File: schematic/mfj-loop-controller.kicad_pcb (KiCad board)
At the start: 4 copper layers, 120.6 x 91.4 mm, 34 parts, among them J1 Adafruit ADS1115, J2 Bias Tee, J3 SWR Bridge, J4 DC+12V, U1 AD8032, U2 R-785.0-1.0, U3 TMR3-1212, U4 WeMos_D1_mini, U5 LCC120, U6 LCC120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

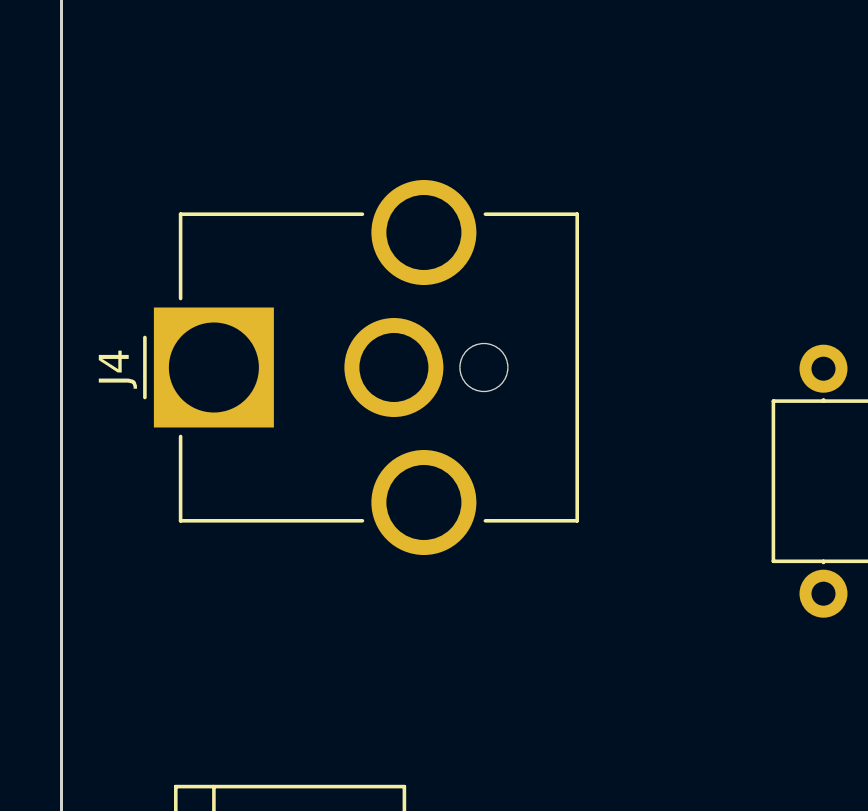
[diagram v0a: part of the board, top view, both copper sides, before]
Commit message: Rotate power jack 180 degrees on PCB.
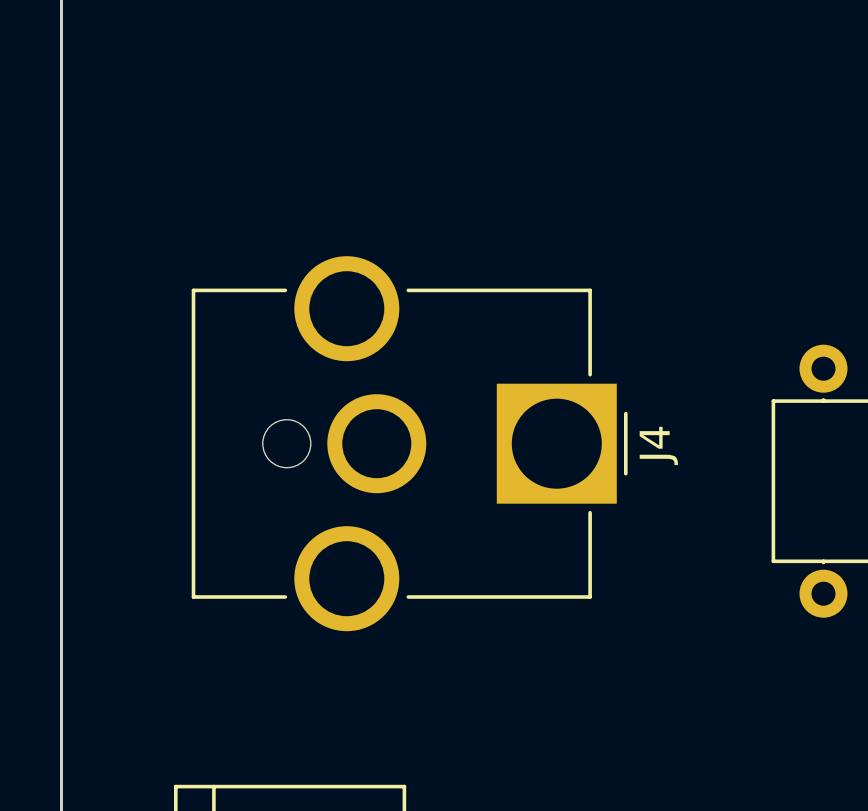
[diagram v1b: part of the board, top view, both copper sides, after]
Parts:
- moved J4 11.7 mm to (74.9, 53.3), turned to 270 degrees

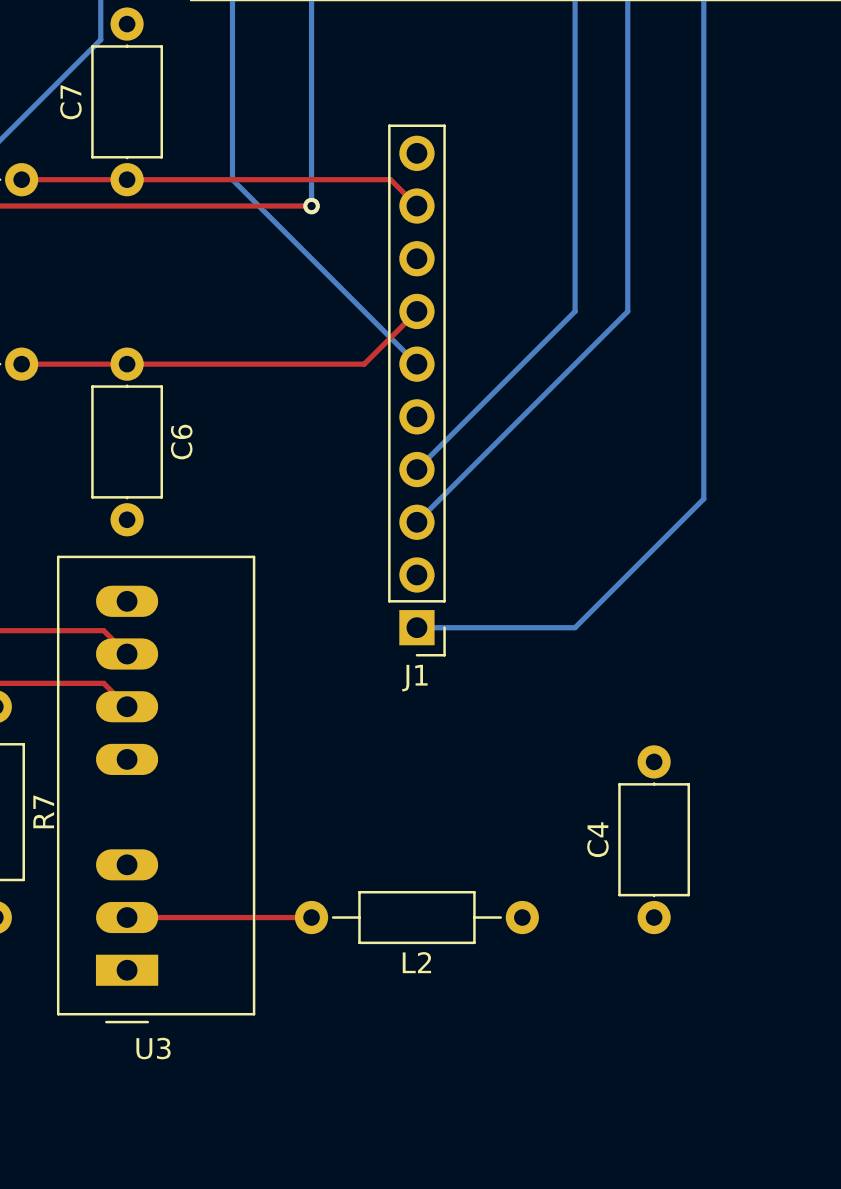
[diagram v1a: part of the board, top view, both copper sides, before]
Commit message: Add minimum load to 12V isolated supply to reduce tuning noise.
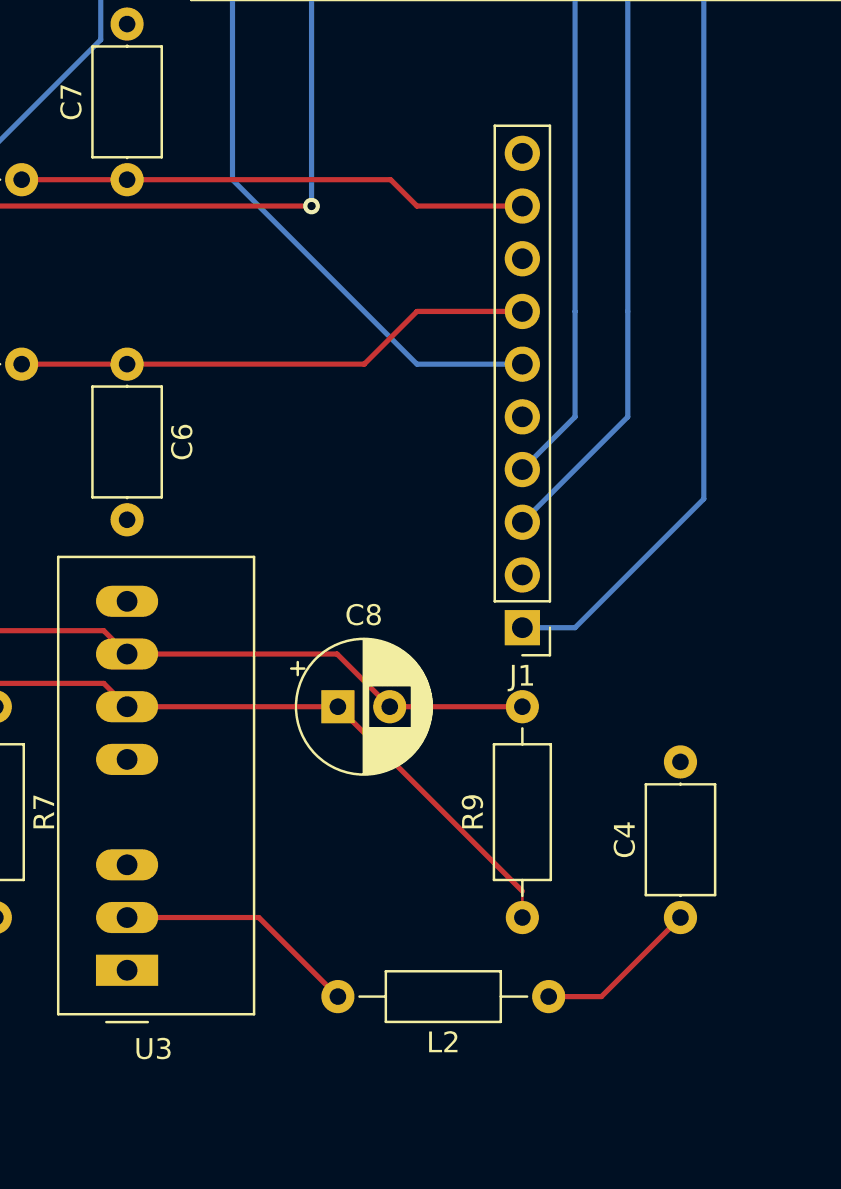
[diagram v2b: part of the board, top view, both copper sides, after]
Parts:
- added C8: 220uF, Capacitor_THT:CP_Radial_D6.3mm_P2.50mm, F.Cu at (142.2, 92.7)
- added R9: 1K, Resistor_THT:R_Axial_DIN0207_L6.3mm_D2.5mm_P10.16mm_Horizontal, F.Cu at (151.1, 102.9)
- moved J1 5.08 mm to (151.1, 88.9)
- moved L2 4.02 mm to (152.4, 106.7)
- moved C4 1.27 mm to (158.8, 102.9)
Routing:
- net /ISOLATED_12V: track 55.9 -> 79.9 mm
- net /ISOLATED_GND: track 53.3 -> 73.4 mm
- net +12V: track 0.06 -> 7.98 mm
- net /POWER_3.3V: track 145.9 -> 140.8 mm
- net Net-(C7-Pad1): track 19.6 -> 24.7 mm
- net Net-(C6-Pad1): track 20.1 -> 25.2 mm
- net /ADC_ALERT: track 55.1 -> 60.2 mm
- net Net-(L2-Pad2): track 8.89 -> 11.7 mm
- net /ADC_SDA: track 27.3 -> 25.2 mm
- net /ADC_SCL: track 30.9 -> 28.8 mm

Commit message: Hardware version 1.2.0:
1. Change 12V isolated supply to "low ripple/noise" version (TVN 3-1212).
2. Add/update required filtering to reflect TVN 3-1212 and to further reduce ripple.
3. Reroute isolated section to shorten traces and to use isolated power/ground planes (EMI reduction).
4. Add optional (?) "minimum load" resistors for use if TVN 3-1212 requires them for proper operation while idle/slow tuning.
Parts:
- added C10: 330nF, Capacitor_THT:C_Axial_L5.1mm_D3.1mm_P7.50mm_Horizontal, F.Cu at (125.7, 100.3)
- added C9: 330nF, Capacitor_THT:C_Axial_L5.1mm_D3.1mm_P7.50mm_Horizontal, F.Cu at (135.9, 100.3)
- added L3: 1mH, Inductor_THT:L_Axial_L5.3mm_D2.2mm_P10.16mm_Horizontal_Vishay_IM-1, F.Cu at (135.9, 104.1)
- added R10: 1000, Resistor_THT:R_Axial_DIN0207_L6.3mm_D2.5mm_P10.16mm_Horizontal, F.Cu at (114.3, 101.6)
- C4: value 2.2uF 25V -> 22uF 25V
- C8: value 220uF -> 22uF 25V; footprint Capacitor_THT:CP_Radial_D6.3mm_P2.50mm -> Capacitor_THT:C_Axial_L5.1mm_D3.1mm_P7.50mm_Horizontal
- L2: value 18uH -> 4.7uH
- R9: value 1K -> 1000
- U3: value TMR3-1212 -> TVN3-1212
- moved U8 33.2 mm to (88.9, 94.0)
- moved R7 31.8 mm to (94.0, 94.0), turned to 90 degrees
- moved R9 31.8 mm to (119.4, 101.6)
- moved U6 21.6 mm to (105.4, 108.0)
- moved R8 20.7 mm to (110.5, 102.9)
- moved REF** 17.1 mm to (158.8, 77.5)
- moved C8 16.2 mm to (153.7, 104.1), turned to 90 degrees
- moved U3 11.4 mm to (142.2, 110.5)
- moved J4 10.2 mm to (64.8, 54.6), turned to 90 degrees
- moved L2 8.98 mm to (161.3, 108.0)
- moved H2 7.62 mm to (167.6, 29.2)
- moved H4 7.62 mm to (167.6, 113.0)
- moved U7 4.02 mm to (105.4, 94.0)
- moved C4 2.84 mm to (161.3, 104.1)
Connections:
- C8 pad 1: /ISOLATED_12V -> Net-(C8-Pad1)
- C8 pad 2: /ISOLATED_GND -> GND
- L2 pad 2: Net-(L2-Pad2) -> Net-(C8-Pad1)
- U3 pad 2: Net-(L2-Pad2) -> Net-(C8-Pad1)
- U3 pad 6: /ISOLATED_12V -> Net-(C9-Pad1)
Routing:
- net /ISOLATED_12V: track 79.9 -> 3.81 mm
- net /ISOLATED_GND: track 73.4 -> 0.00 mm
- net /BIAS_L: track 60.5 -> 26.9 mm
- net /BIAS_R: track 33.5 -> 50.8 mm, vias 0 -> 2
- net Net-(C8-Pad1): track 0.00 -> 13.8 mm
- net Net-(L2-Pad2): track 11.7 -> 0.00 mm
- net Net-(C9-Pad1): track 0.00 -> 11.2 mm
- net /GPIO_TUNE_UP: track 119.1 -> 108.7 mm
- net +12V: track 7.98 -> 0.00 mm
- net /GPIO_TUNE_DOWN: track 99.9 -> 93.5 mm, vias 4 -> 6
- net Net-(U5-Pad3): track 12.4 -> 17.6 mm
- net Net-(U7-Pad3): track 24.2 -> 20.6 mm, vias 2 -> 0
- net Net-(R7-Pad1): track 3.81 -> 7.18 mm
- net Net-(R8-Pad1): track 6.35 -> 5.08 mm
- added copper zone on In2.Cu, net /ISOLATED_12V
- added copper zone on In1.Cu, net /ISOLATED_GND
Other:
- board size 120.6 x 91.4 mm -> 113 x 91.4 mm
- net class Default: trace_width 0.127 -> 0.25; via_dia 0.4572 -> 0.8; via_drill 0.254 -> 0.4
- rule trace_min: 0.127 -> 0.25
- rule via_min_drill: 0.254 -> 0.4
- rule via_min_size: 0.4572 -> 0.8
- board text added: "MFJ Wi-Fi Loop Controller v1.2.0 https://github.com/tmiw/MFJLoopController"
- board text removed: "MFJ Wi-Fi Loop Controller v1.1.0 https://github.com/tmiw/MFJLoopController"
